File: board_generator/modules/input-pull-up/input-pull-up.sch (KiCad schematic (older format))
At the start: 6 parts, among them J1 Screw_Terminal_1x01, X1 interface, X2 interface

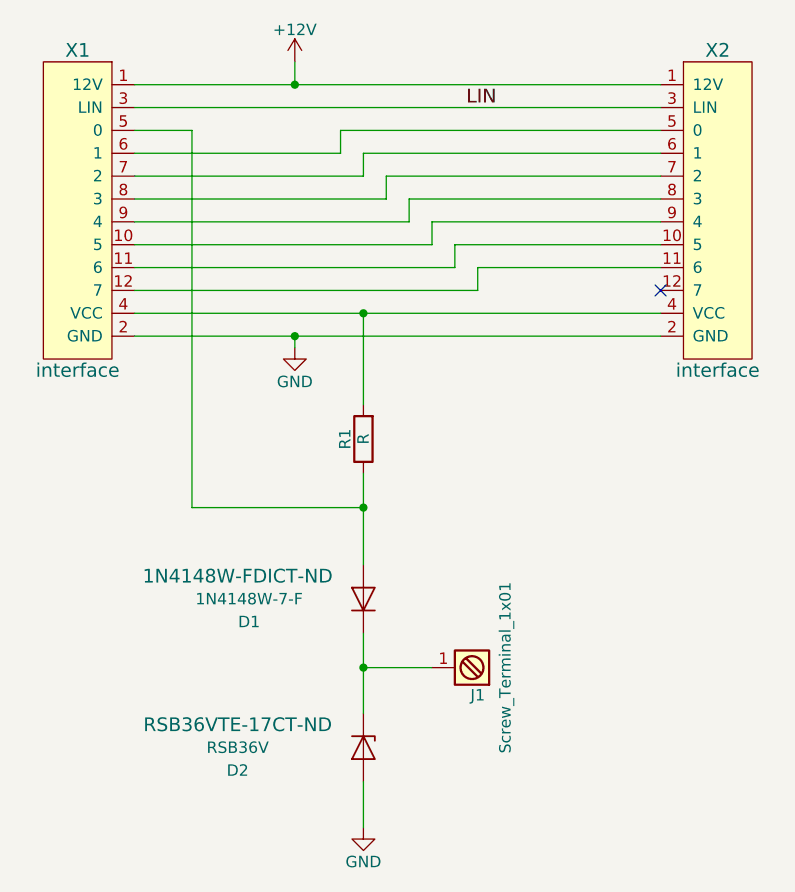
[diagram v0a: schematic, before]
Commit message: Adding value and DigiKey reference for R1 on input-pull-up
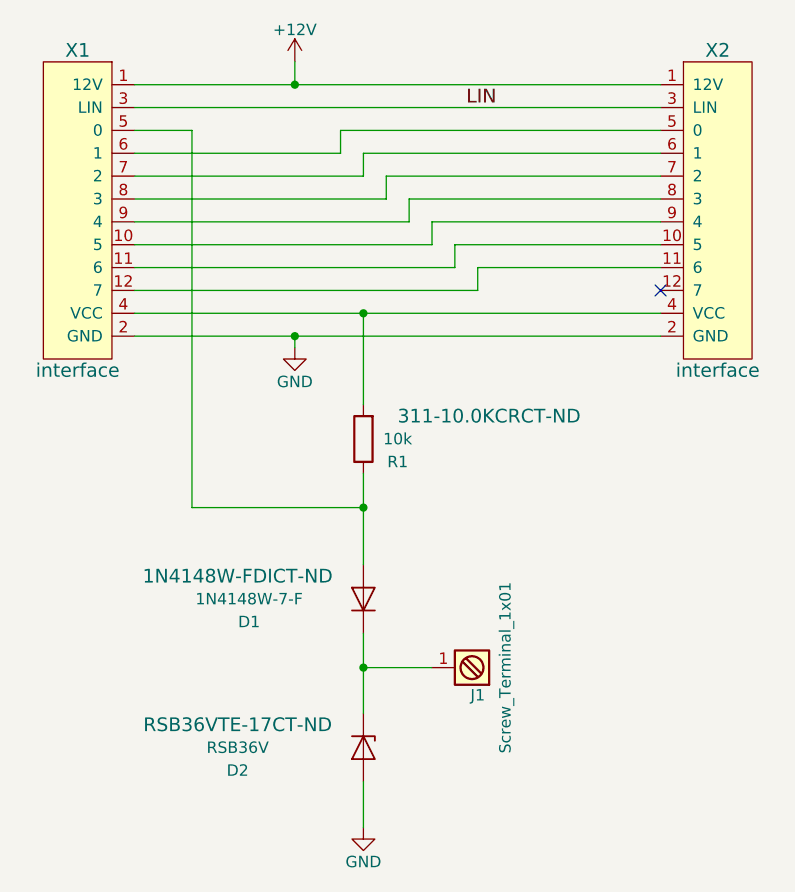
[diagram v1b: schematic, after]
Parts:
- R1: value R -> 10k; DIGIKEY (none) -> 311-10.0KCRCT-ND
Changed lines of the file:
@@
 U 1 1 597E6F52
 P 6050 4100
-F 0 "R1" V 6130 4100 50  0000 C CNN
-F 1 "R" V 6050 4100 50  0000 C CNN
+F 0 "R1" H 5900 4200 50  0000 C CNN
+F 1 "10k" H 5900 4100 50  0000 C CNN
 F 2 "Resistors_SMD:R_0805" V 5980 4100 50  0001 C CNN
 F 3 "" H 6050 4100 50  0001 C CNN
+F 4 "311-10.0KCRCT-ND" H 5500 4000 60  0000 C CNN "DIGIKEY"
 	1    6050 4100
 	-1   0    0    1

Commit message: Using solder pads for module input_pull_up
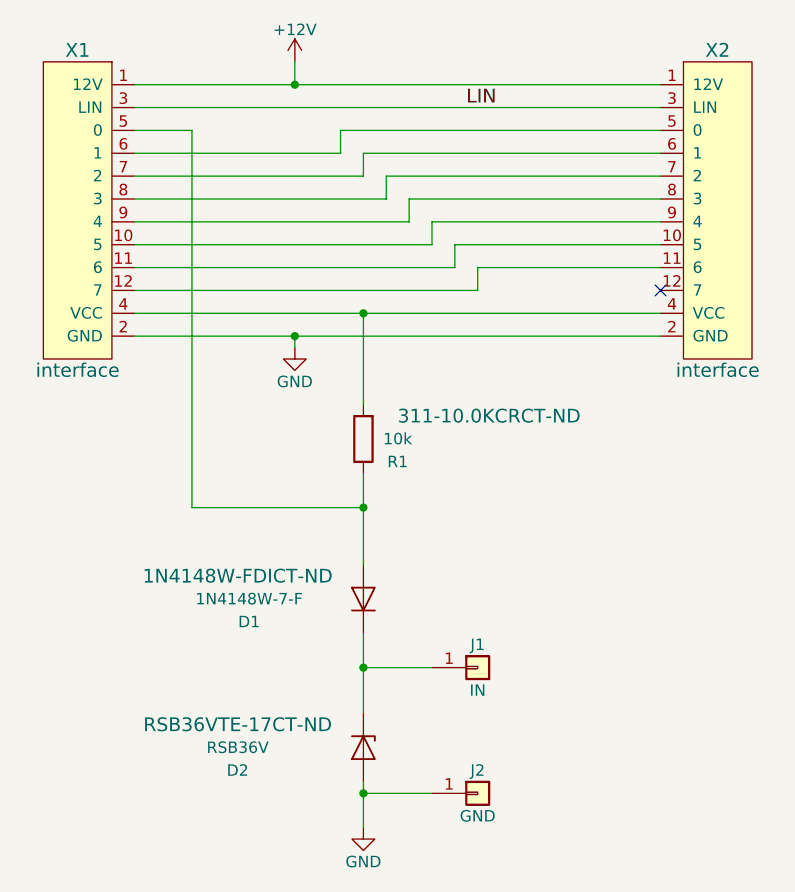
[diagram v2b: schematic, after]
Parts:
- removed J1: Screw_Terminal_1x01, connectors:TERM_SCREW_M3, symbol Screw_Terminal_1x01
- added J1: IN, connectors:SolderWirePad_single_SMD_15x40mil, symbol Conn_01x01
- added J2: GND, connectors:SolderWirePad_single_SMD_15x40mil, symbol Conn_01x01
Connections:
- net GND: now also J2.1 (Pin_1)
- net at D1.1 (K), D2.1 (K): now also J1.1 (Pin_1)
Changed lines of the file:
@@
 Wire Wire Line
 	5050 3550 7350 3550
-$Comp
-L Screw_Terminal_1x01 J1
-U 1 1 597E743F
-P 6550 5100
-F 0 "J1" H 6550 5250 50  0000 C TNN
-F 1 "Screw_Terminal_1x01" V 6400 5100 50  0000 C TNN
-F 2 "connectors:TERM_SCREW_M3" H 6550 4975 50  0001 C CNN
-F 3 "" H 6550 5000 50  0001 C CNN
-	1    6550 5100
-	-1   0    0    1
-$EndComp
 Wire Wire Line
 	6050 4250 6050 4650
@@
 Wire Wire Line
 	5300 4400 6050 4400
+$Comp
+L Conn_01x01 J1
+U 1 1 5BDFDC83
+P 6550 5100
+F 0 "J1" H 6550 5200 50  0000 C CNN
+F 1 "IN" H 6550 5000 50  0000 C CNN
+F 2 "connectors:SolderWirePad_single_SMD_15x40mil" H 6550 5100 50  0001 C CNN
+F 3 "" H 6550 5100 50  0001 C CNN
+	1    6550 5100
+	1    0    0    -1
+$EndComp
+$Comp
+L Conn_01x01 J2
+U 1 1 5BDFDCE4
+P 6550 5650
+F 0 "J2" H 6550 5750 50  0000 C CNN
+F 1 "GND" H 6550 5550 50  0000 C CNN
+F 2 "connectors:SolderWirePad_single_SMD_15x40mil" H 6550 5650 50  0001 C CNN
+F 3 "" H 6550 5650 50  0001 C CNN
+	1    6550 5650
+	1    0    0    -1
+$EndComp
+Wire Wire Line
+	6350 5650 6050 5650
+Connection ~ 6050 5650
 $EndSCHEMATC
